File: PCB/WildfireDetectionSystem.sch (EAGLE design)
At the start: 61 parts, among them IC1 STM32L476RGT6, J1 10118192-0001LF, J3 B4B-XH-A, J4 B5B-XH-A, SW1 1825910-6, U1 BME280, U2 LD39050PU33R, U3 NEO-6M-GPS, U4 24AA32A-I/MS, Y1 ABLS-8.000MHZ-B2-T, Y2 ECS-.327-12.5-12QS-TR

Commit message: board and schematic changes
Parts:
- removed C15, C16, C17, C18: CC0402KRX7R7BB104, ce-capstone:CC0402KRX7R7BB104
- removed U4: 24AA32A-I/MS, 24AA32A-I_MS:24AA32A-I/MS
- added C1, C23: CL05B104KO5NNNC, CL05B104KO5NNNC:CL05B104KO5NNNC
- added C24, C25: CL10C200JB8NNNC, CL10C200JB8NNNC:CL10C200JB8NNNC
- added U$1: 24LC32AT-I/SN, 24LC32AT-I_SN:24LC32AT-I/SN
- C11, C12, C13, C14: value CC0402KRX7R7BB104 -> CL05B104KO5NNNC; device ce-capstone:CC0402KRX7R7BB104 -> CL05B104KO5NNNC:CL05B104KO5NNNC
- C2, C21: value CC0402KRX7R7BB104 -> CL10C200JB8NNNC; device ce-capstone:CC0402KRX7R7BB104 -> CL10C200JB8NNNC:CL10C200JB8NNNC
- C6, C7, C8, C9: value CC0402JRNPO9BN200 -> CL05B104KO5NNNC; device ce-capstone:CC0402JRNPO9BN200 -> CL05B104KO5NNNC:CL05B104KO5NNNC
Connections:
- net 3V3: now also C6.1, C7.1, C8.1, C9.1, U$1.VCC; no longer C13.1, C14.1, C15.1, C16.1, U4.VCC
- net 5V: now also C23.1; no longer C2.1
- net GND: now also C1.2, C21.2, C23.2, C24.2, C25.2, U$1.A0, U$1.A1, U$1.A2, U$1.VSS, U$1.WP; no longer C15.2, C16.2, C17.2, C18.2, C21.1, U4.A0, U4.A1, U4.A2, U4.VSS, U4.WP
- net GPS_SCL: now also U$1.SCL; no longer U4.SCL
- net GPS_SDA: now also U$1.SDA; no longer U4.SDA
- net NRST: now also C1.1; no longer C21.2
- net PC14-OSC32-IN: now also C24.1; no longer C8.1
- net PC15-OSC32-OUT: now also C25.1; no longer C9.1
- net PH0-OSC-IN: now also C2.1; no longer C6.1
- net PH1-OSC-OUT: now also C21.1; no longer C7.1
- net VREF_PLUS: now also C13.1, C14.1; no longer C17.1, C18.1
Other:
- moved on the sheet: C11, C12, C13, C14, C2, C21, C6, C7, C8, C9

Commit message: pcb v2
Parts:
- removed ANTENNA: (no value), discrete:ANTENNA
- added BATTERY: (no value), con-lstb:MA03-1
- added C15, C17: 4.7uF, rcl:C-USC0603
- added C16, C30: 1uF, rcl:C-USC0603
- added C18, C26, C27, C28, C33, C34, C36: 22uF, rcl:C-USC0603
- added C29: .1uF, rcl:C-USC0603
- added C31: 220nF, rcl:C-USC0603
- added C32, C35, C37: 10uF, rcl:C-USC0603
- added C38: 3.3nF, rcl:C-USC0603
- added D6: SML-P12MTT86, ce-capstone:SML-P12MTT86
- added D7: SML-P12VTT86, ce-capstone:SML-P12VTT86
- added J7: B4B-PH-K-S, B4B-PH-K-S:B4B-PH-K-S
- added J8: U.FL-R-SMT-1(10), U.FL-R-SMT-1_10_:U.FL-R-SMT-1(10)
- added J9: B2B-PH-K-S, B2B-PH-K-S:B2B-PH-K-S
- added L2: 8uH, rcl:L-USL3225M
- added L3: 1uH, rcl:L-USL3225M
- added L4: 2.2uH, rcl:L-USL3225M
- added R13: 1.18k, rcl:R-US_R0603
- added R14: 1.13k, rcl:R-US_R0603
- added R15, R16: 1k, rcl:R-US_R0603
- added R17, R18, R21, R22: 100k, rcl:R-US_R0603
- added R19: 24.9k, rcl:R-US_R0603
- added R20: 732k, rcl:R-US_R0603
- added STLINK_INTERFACE: (no value), con-lstb:MA03-2
- added U$5: NC_MARKER, NC_MARKER:NC_MARKER
- added U4: TPS62142RGTT, TPS62142RGTT:TPS62142RGTT
- added U5: TPS61022RWUR, TPS61022RWUR:TPS61022RWUR
- added U6: LMR33630ADDA, LMR33630ADDA:LMR33630ADDA
- added U7: BQ24074RGTR, BQ24074RGTR:BQ24074RGTR
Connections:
- new net BAT: BATTERY.1, C15.1, U7.BAT_2, U7.BAT_3
- new net BOOT: C29.2, U6.BOOT
- new net CHG: D6.C, U7.!CHG
- new net FB: R17.2, R19.1, U6.FB
- new net FB2: R20.2, R21.1, U5.FB
- new net ILIM: R13.2, U7.ILIM
- new net ISET: R14.2, U7.ISET
- new net N$17: D6.A, R16.1
- new net N$18: D7.A, R15.1
- new net N$28: U$5.P$1, U7.ITERM
- new net PG: R22.1, U4.PG
- new net PG2: R18.1, U6.PG
- new net PGOOD: D7.C, U7.!PGOOD
- new net SOLAR_IN: C31.1, C32.1, J9.2, U6.EN, U6.VIN
- new net SS/TR: C38.1, U4.SS/TR
- new net SW: L4.1, U4.SW
- new net SW2: L3.1, U5.SW
- new net SW3: C29.1, L2.2, U6.SW
- new net SWCLK: IC1.PA14(JTCK-SWCLK), STLINK_INTERFACE.4
- new net SWDIO: IC1.PA13(JTMS-SWDIO), STLINK_INTERFACE.6
- new net SYS: C17.1, C35.1, C37.1, L3.2, R15.2, R16.2, U4.AVIN, U4.EN, U4.PVIN, U5.EN, U5.VIN, U7.EN2, U7.OUT_10, U7.OUT_11
- new net TRACESWO: IC1.PB3(JTDO-TRACESWO), STLINK_INTERFACE.2
- new net TS: BATTERY.3, U7.TS
- new net VCC: C30.1, R18.2, U6.VCC
- net 3V3: now also C36.1, J7.1, L4.2, R22.2, STLINK_INTERFACE.5, U4.VOS; no longer SV1.4
- net 5V: now also C33.1, C34.1, R20.1, SV1.4, U5.VOUT
- net 5V_IN: now also C16.1, C18.1, C26.1, C27.1, C28.1, L2.1, R17.1, U7.IN
- net GND: now also BATTERY.2, C15.2, C16.2, C17.2, C18.2, C26.2, C27.2, C28.2, C30.2, C31.2, C32.2, C33.2, C34.2, C35.2, C36.2, C37.2, C38.2, J7.4, J8.GND, J9.1, R13.1, R14.1, R19.2, R21.2, STLINK_INTERFACE.1, U4.AGND, U4.DEF, U4.EXP, U4.FB, U4.FSW, U4.PGND, U5.GND, U5.MODE, U6.AGND, U6.PGND, U7.!CE, U7.EN1, U7.EXP, U7.TMR, U7.VSS
- net NRST: now also STLINK_INTERFACE.3
- net RF_IN: now also J8.SIG; no longer ANTENNA.1
- net UART1_RX_LORA: now also J4.4; no longer J4.3
- net UART1_TX_LORA: now also J4.3; no longer J4.4
- net UART3_RX_GPS: now also J7.3
- net UART3_TX_GPS: now also J7.2
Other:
- moved on the sheet: J3, J4, SV2

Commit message: pcbv2
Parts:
- removed C23: CL05B104KO5NNNC, CL05B104KO5NNNC:CL05B104KO5NNNC
- removed C3: CC0402KRX7R7BB104, ce-capstone:CC0402KRX7R7BB104
- removed C4, C5: CC0603KRX5R7BB105, ce-capstone:CC0603KRX5R7BB105
- removed D3: SML-P12MTT86, ce-capstone:SML-P12MTT86
- removed R6: RC0402FR-071KL, ce-capstone:RC0402FR-071KL
- removed U$2: STPS1L30A, ce-capstone:STPS1L30A
- removed U2: LD39050PU33R, ce-capstone:LD39050PU33R
- added D10, D8, D9: SS34LWH, SS34LWH:SS34LWH
- added R23: 10k, rcl:R-US_R0603
- BT1: value MS621FE-FL11E -> 1056TR; device MS621FE-FL11E:MS621FE-FL11E -> 1056TR:1056TR
- SW1: value 1825910-6 -> 434133025816; device ce-capstone:1825910-6 -> 434133025816:434133025816
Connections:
- removed net N$1: D3.A, R6.1
- new net 5V_IN_SOLAR: C18.1, C26.1, C27.1, C28.1, D9.A, L2.1, R17.1
- new net 5V_IN_USB: D10.A, J1.VUSB
- new net N$15: D8.K, U6.EN, U6.VIN
- net 3V3: no longer C3.1, C4.1, R6.2, U2.VOUT
- net 5V: no longer C23.1, C5.1, U$2.C, U2.EN, U2.VIN
- net 5V_IN: now also D10.K, D9.K, R16.2; no longer C18.1, C26.1, C27.1, C28.1, J1.VUSB, L2.1, R17.1, U$2.A
- net GND: now also BT1.NEG, R23.1; no longer BT1.-, C23.2, C3.2, C4.2, C5.2, D3.C, U2.GND
- net N$10: now also BT1.POS; no longer BT1.+
- net SOLAR_IN: now also D8.A; no longer U6.EN, U6.VIN
- net SYS: no longer R16.2
- net TS: now also R23.2; no longer BATTERY.3
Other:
- moved on the sheet: C1

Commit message: pcbv2
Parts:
- removed L2: 8uH, rcl:L-USL3225M
- added C3: 22uF, JLC PCB Basic Parts_loc:C_22UF/6.3V_0603
- added L5: L_4R7_0603, JLC PCB Basic Parts_loc:L_4R7_0603
- added L6: L_2R2_0805, JLC PCB Basic Parts_loc:L_2R2_0805
- C15: device rcl:C-USC0603 -> JLC PCB Basic Parts_loc:C_4.7PF/50V_0603
- C16, C30: device rcl:C-USC0603 -> JLC PCB Basic Parts_loc:C_1UF/50V_0603
- C17: device rcl:C-USC0603 -> JLC PCB Basic Parts_loc:C_4.7UF/16V_0603
- C18, C26, C27, C28, C33, C34, C36: device rcl:C-USC0603 -> JLC PCB Basic Parts_loc:C_22UF/6.3V_0603
- C29: device rcl:C-USC0603 -> JLC PCB Basic Parts_loc:C_100NF/50V_0603
- C31: device rcl:C-USC0603 -> JLC PCB Basic Parts_loc:C_220NF/25V_0603
- C32, C35, C37: device rcl:C-USC0603 -> JLC PCB Basic Parts_loc:C_10UF/10V_0603
- C38: device rcl:C-USC0603 -> JLC PCB Basic Parts_loc:C_3.3NF/50V_0603
- L3: device rcl:L-USL3225M -> JLC PCB Basic Parts_loc:L_1R0_0805
- L4: device rcl:L-USL3225M -> JLC PCB Basic Parts_loc:L_2R2_0805
- R13: LCSC_PART (none) -> C861193
- R14: LCSC_PART (none) -> C137782
- R15, R16: device rcl:R-US_R0603 -> JLC PCB Basic Parts_loc:R_1K_0603
- R17, R18, R21, R22: device rcl:R-US_R0603 -> JLC PCB Basic Parts_loc:R_100K_0603
- R19: LCSC_PART (none) -> C2654014
- R20: LCSC_PART (none) -> C403344
- R23: device rcl:R-US_R0603 -> JLC PCB Basic Parts_loc:R_10K_0603
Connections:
- new net N$1: L5.2, L6.1
- net 5V: now also C3.1
- net 5V_IN_SOLAR: now also L5.1; no longer L2.1
- net GND: now also C3.2
- net SW3: now also L6.2; no longer L2.2

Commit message: pcbv2
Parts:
- added L2: L_1R0_0805, JLC PCB Basic Parts_loc:L_1R0_0805
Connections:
- new net N$16: L2.2, L6.2
- net SW3: now also L2.1; no longer L6.2
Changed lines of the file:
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@@
 <part name="L5" library="JLC PCB Basic Parts_loc" deviceset="L_" device="_0603" package3d_urn="urn:adsk.eagle:package:23555/3" technology="4R7"/>
 <part name="L6" library="JLC PCB Basic Parts_loc" deviceset="L_" device="_0805" package3d_urn="urn:adsk.eagle:package:23553/2" technology="2R2"/>
+<part name="L2" library="JLC PCB Basic Parts_loc" deviceset="L_" device="_0805" package3d_urn="urn:adsk.eagle:package:23553/2" technology="1R0"/>
 </parts>
 <sheets>
@@
 <attribute name="NAME" x="341.4014" y="92.71" size="1.778" layer="95" rot="R90"/>
 <attribute name="VALUE" x="346.202" y="92.71" size="1.778" layer="96" rot="R90"/>
+</instance>
+<instance part="L2" gate="L1" x="347.98" y="86.36" smashed="yes" rot="R270">
+<attribute name="NAME" x="344.17" y="87.8586" size="1.778" layer="95"/>
+<attribute name="VALUE" x="344.17" y="83.058" size="1.778" layer="96"/>
 </instance>
 </instances>
@@
 <wire x1="350.52" y1="104.14" x2="347.98" y2="104.14" width="0.1524" layer="91"/>
 <label x="353.06" y="99.06" size="1.778" layer="95"/>
-<pinref part="L6" gate="L1" pin="2"/>
-<wire x1="342.9" y1="91.44" x2="347.98" y2="91.44" width="0.1524" layer="91"/>
 <wire x1="347.98" y1="91.44" x2="347.98" y2="99.06" width="0.1524" layer="91"/>
 <junction x="347.98" y="99.06"/>
+<pinref part="L2" gate="L1" pin="1"/>
+<wire x1="353.06" y1="86.36" x2="353.06" y2="91.44" width="0.1524" layer="91"/>
+<wire x1="353.06" y1="91.44" x2="347.98" y2="91.44" width="0.1524" layer="91"/>
 </segment>
 </net>
@@
 </segment>
 </net>
+<net name="N$16" class="0">
+<segment>
+<pinref part="L6" gate="L1" pin="2"/>
+<pinref part="L2" gate="L1" pin="2"/>
+<wire x1="342.9" y1="91.44" x2="342.9" y2="86.36" width="0.1524" layer="91"/>
+</segment>
+</net>

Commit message: pcbv2
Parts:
- added C23, C39: C_10UF/25V_0805, JLC PCB Basic Parts_loc:C_10UF/25V_0805
- added C4, C5: C_10UF/10V_0603, JLC PCB Basic Parts_loc:C_10UF/10V_0603
- added C40, C41, C42: C_22UF/25V_0805, JLC PCB Basic Parts_loc:C_22UF/25V_0805
- added C43: C_100NF/50V_0603, JLC PCB Basic Parts_loc:C_100NF/50V_0603
- added L8: L_1R0_0805, JLC PCB Basic Parts_loc:L_1R0_0805
- added R24: R_100K_0603, JLC PCB Basic Parts_loc:R_100K_0603
- added R25: R_680K_0603, JLC PCB Basic Parts_loc:R_680K_0603
- added R26: R_130K_0603, JLC PCB Basic Parts_loc:R_130K_0603
- added R6: R_10K_0603, JLC PCB Basic Parts_loc:R_10K_0603
- added U2: TPS63070RNMR, TPS63070RNMR:TPS63070RNMR
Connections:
- new net 5V_BUCK: C16.1, C4.2, C40.1, C41.1, C42.1, R24.2, R25.1, U2.VOUT, U7.IN
- new net N$19: L8.1, U2.L1
- new net N$20: L8.2, U2.L2
- new net N$21: R6.1, U2.EN, U2.PS/SYNC
- new net N$22: R24.1, U2.PG
- new net N$23: R25.2, R26.2, U2.FB
- new net VAUX: C43.1, U2.VAUX
- net 5V_IN: now also C23.1, C39.1, C5.2, R6.2, U2.VIN; no longer C16.1, U7.IN
- net GND: now also C23.2, C39.2, C4.1, C40.2, C41.2, C42.2, C43.2, C5.1, R26.1, U2.FB2, U2.GND, U2.PGND, U2.VSEL
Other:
- moved on the sheet: BATTERY, C15, C16, C17, C3, C33, C34, C35, C36, C37, C38, D6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

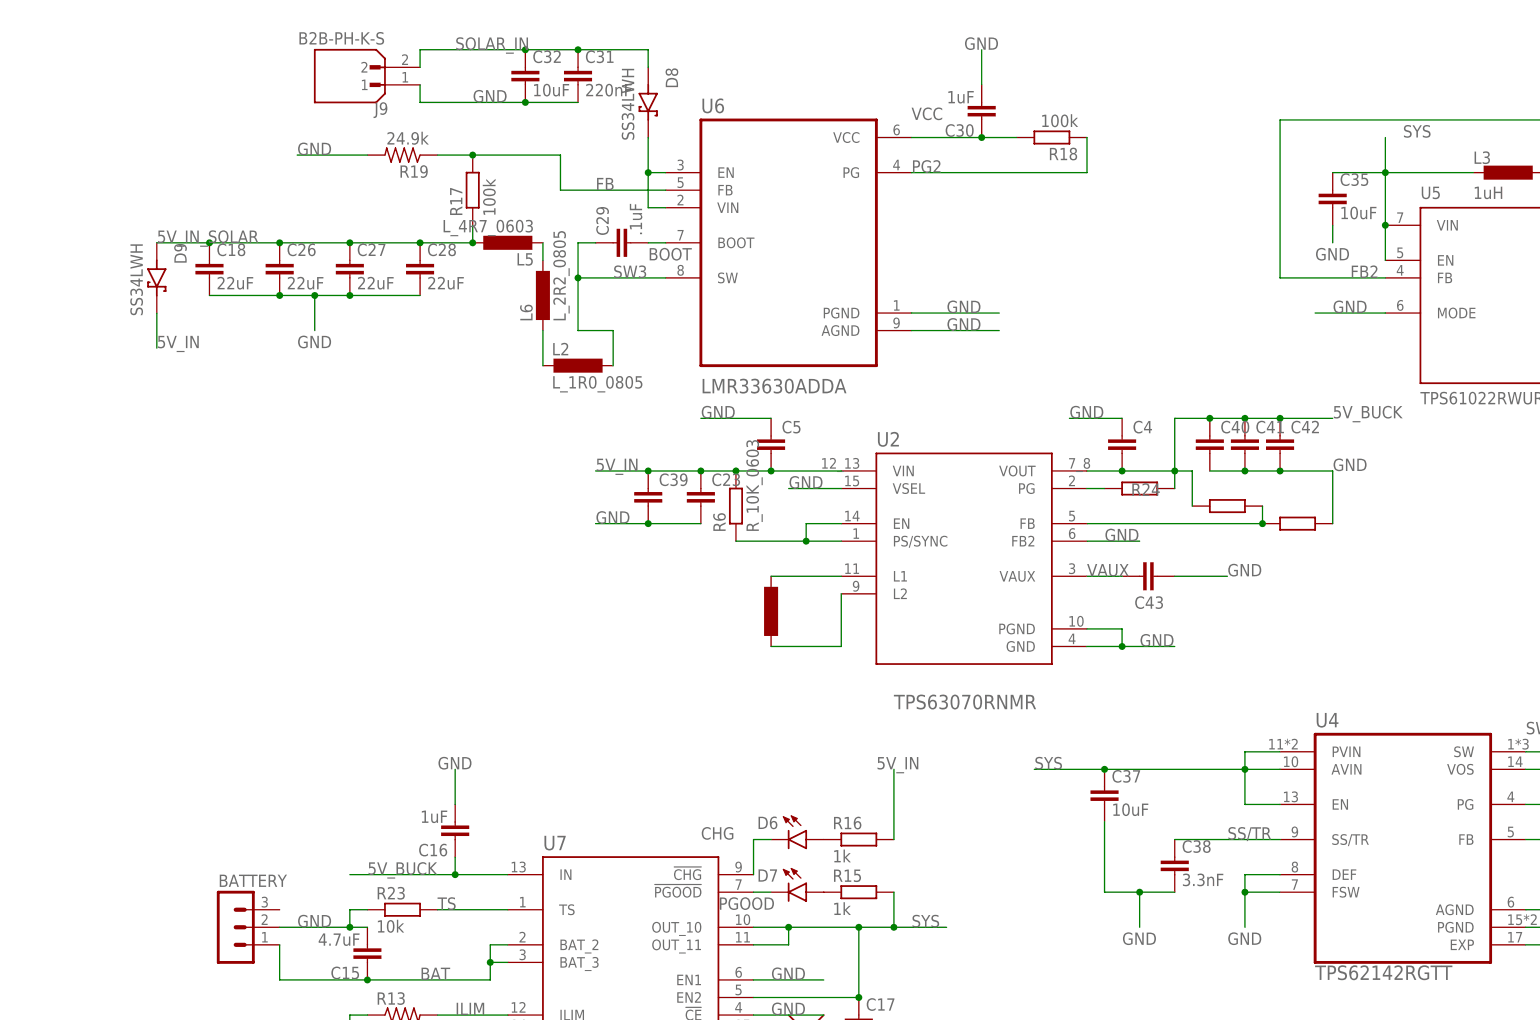
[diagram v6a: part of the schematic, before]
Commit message: changed charging circuit to add buck/boost
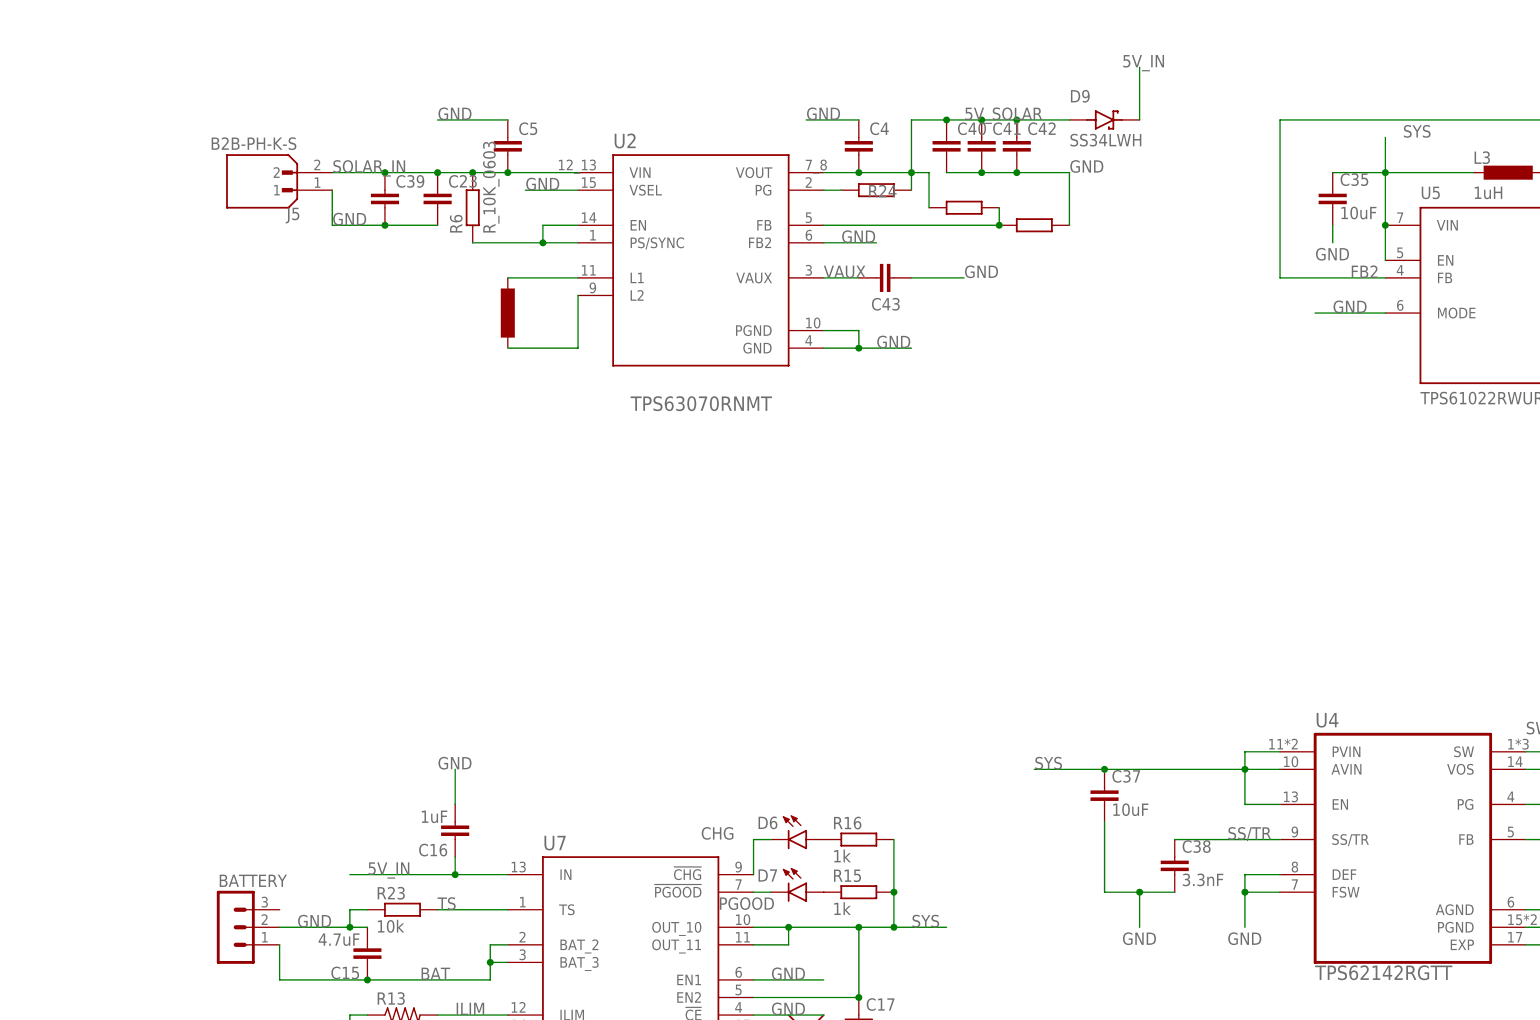
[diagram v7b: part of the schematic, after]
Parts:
- removed C18, C26, C27, C28: 22uF, JLC PCB Basic Parts_loc:C_22UF/6.3V_0603
- removed C29: .1uF, JLC PCB Basic Parts_loc:C_100NF/50V_0603
- removed C30: 1uF, JLC PCB Basic Parts_loc:C_1UF/50V_0603
- removed C31: 220nF, JLC PCB Basic Parts_loc:C_220NF/25V_0603
- removed C32: 10uF, JLC PCB Basic Parts_loc:C_10UF/10V_0603
- removed D8: SS34LWH, SS34LWH:SS34LWH
- removed J9: B2B-PH-K-S, B2B-PH-K-S:B2B-PH-K-S
- removed L2: L_1R0_0805, JLC PCB Basic Parts_loc:L_1R0_0805
- removed L5: L_4R7_0603, JLC PCB Basic Parts_loc:L_4R7_0603
- removed L6: L_2R2_0805, JLC PCB Basic Parts_loc:L_2R2_0805
- removed R17, R18: 100k, JLC PCB Basic Parts_loc:R_100K_0603
- removed R19: 24.9k, rcl:R-US_R0603
- removed U6: LMR33630ADDA, LMR33630ADDA:LMR33630ADDA
- added J5: B2B-PH-K-S, B2B-PH-K-S:B2B-PH-K-S
- U2: value TPS63070RNMR -> TPS63070RNMT; device TPS63070RNMR:TPS63070RNMR -> TPS63070RNMT:TPS63070RNMT
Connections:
- removed net 5V_BUCK: C16.1, C4.2, C40.1, C41.1, C42.1, R24.2, R25.1, U2.VOUT, U7.IN
- removed net 5V_IN_SOLAR: C18.1, C26.1, C27.1, C28.1, D9.A, L5.1, R17.1
- removed net BOOT: C29.2, U6.BOOT
- removed net FB: R17.2, R19.1, U6.FB
- removed net N$1: L5.2, L6.1
- removed net N$15: D8.K, U6.EN, U6.VIN
- removed net N$16: L2.2, L6.2
- removed net PG2: R18.1, U6.PG
- removed net SW3: C29.1, L2.1, U6.SW
- removed net VCC: C30.1, R18.2, U6.VCC
- new net 5V_SOLAR: C4.2, C40.1, C41.1, C42.1, D9.A, R24.2, R25.1, U2.VOUT
- net 5V_IN: now also C16.1, U7.IN; no longer C23.1, C39.1, C5.2, R16.2, R6.2, U2.VIN
- net GND: now also J5.1; no longer C18.2, C26.2, C27.2, C28.2, C30.2, C31.2, C32.2, J9.1, R19.2, U6.AGND, U6.PGND
- net SOLAR_IN: now also C23.1, C39.1, C5.2, J5.2, R6.2, U2.VIN; no longer C31.1, C32.1, D8.A, J9.2
- net SYS: now also R16.2
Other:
- moved on the sheet: C23, C39, C4, C40, C41, C42, C43, C5, D9, R24, R6, U2

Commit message: inductor change
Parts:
- removed L8: L_1R0_0805, JLC PCB Basic Parts_loc:L_1R0_0805
- added L2: DFE252012P-1R5M=P2, DFE252012P-1R5M_P2:DFE252012P-1R5M=P2
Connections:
- net N$19: now also L2.2; no longer L8.1
- net N$20: now also L2.1; no longer L8.2
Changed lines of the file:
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@@
 <part name="R25" library="JLC PCB Basic Parts_loc" deviceset="R_" device="_0603" package3d_urn="urn:adsk.eagle:package:23555/3" technology="680K"/>
 <part name="R26" library="JLC PCB Basic Parts_loc" deviceset="R_" device="_0603" package3d_urn="urn:adsk.eagle:package:23555/3" technology="130K"/>
-<part name="L8" library="JLC PCB Basic Parts_loc" deviceset="L_" device="_0805" package3d_urn="urn:adsk.eagle:package:23553/2" technology="1R0"/>
 <part name="J5" library="B2B-PH-K-S" deviceset="B2B-PH-K-S" device=""/>
+<part name="L2" library="DFE252012P-1R5M_P2" deviceset="DFE252012P-1R5M=P2" device=""/>
 </parts>
 <sheets>
@@
 <instance part="R25" gate="R1" x="403.86" y="109.22" smashed="yes"/>
 <instance part="R26" gate="R1" x="414.02" y="106.68" smashed="yes" rot="R180"/>
-<instance part="L8" gate="L1" x="337.82" y="93.98" smashed="yes"/>
 <instance part="J5" gate="G$1" x="302.26" y="114.3" smashed="yes" rot="R180">
 <attribute name="NAME" x="307.84" y="109.22" size="1.778" layer="95" rot="R180"/>
 <attribute name="VALUE" x="307.34" y="119.38" size="1.778" layer="96" rot="R180"/>
+</instance>
+<instance part="L2" gate="G$1" x="335.28" y="91.44" smashed="yes" rot="R90">
+<attribute name="NAME" x="330.2" y="83.82" size="1.778" layer="95" rot="R90"/>
+<attribute name="VALUE" x="332.74" y="83.82" size="1.778" layer="96" rot="R90"/>
 </instance>
 </instances>
@@
 <segment>
 <pinref part="U2" gate="G$1" pin="L1"/>
-<wire x1="347.98" y1="99.06" x2="337.82" y2="99.06" width="0.1524" layer="91"/>
-<pinref part="L8" gate="L1" pin="1"/>
+<wire x1="347.98" y1="99.06" x2="335.28" y2="99.06" width="0.1524" layer="91"/>
+<pinref part="L2" gate="G$1" pin="2"/>
 </segment>
 </net>
@@
 <segment>
 <pinref part="U2" gate="G$1" pin="L2"/>
-<pinref part="L8" gate="L1" pin="2"/>
-<wire x1="347.98" y1="88.9" x2="347.98" y2="96.52" width="0.1524" layer="91"/>
-<wire x1="337.82" y1="88.9" x2="347.98" y2="88.9" width="0.1524" layer="91"/>
-</segment>
-</net>
+<wire x1="347.98" y1="83.82" x2="347.98" y2="96.52" width="0.1524" layer="91"/>
+<wire x1="335.28" y1="83.82" x2="347.98" y2="83.82" width="0.1524" layer="91"/>
+<pinref part="L2" gate="G$1" pin="1"/>
+</segment>
+</net>
